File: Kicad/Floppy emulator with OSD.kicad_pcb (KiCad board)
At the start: 2 copper layers, 44.5 x 45.7 mm, 59 parts, among them J1 Display, J10 KBD, J11 Drive Select, J2 SDCARD, J3 Prog, J4 Serial, J5 Prog2, J9 Video, P1 To Computer, P2 POWER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

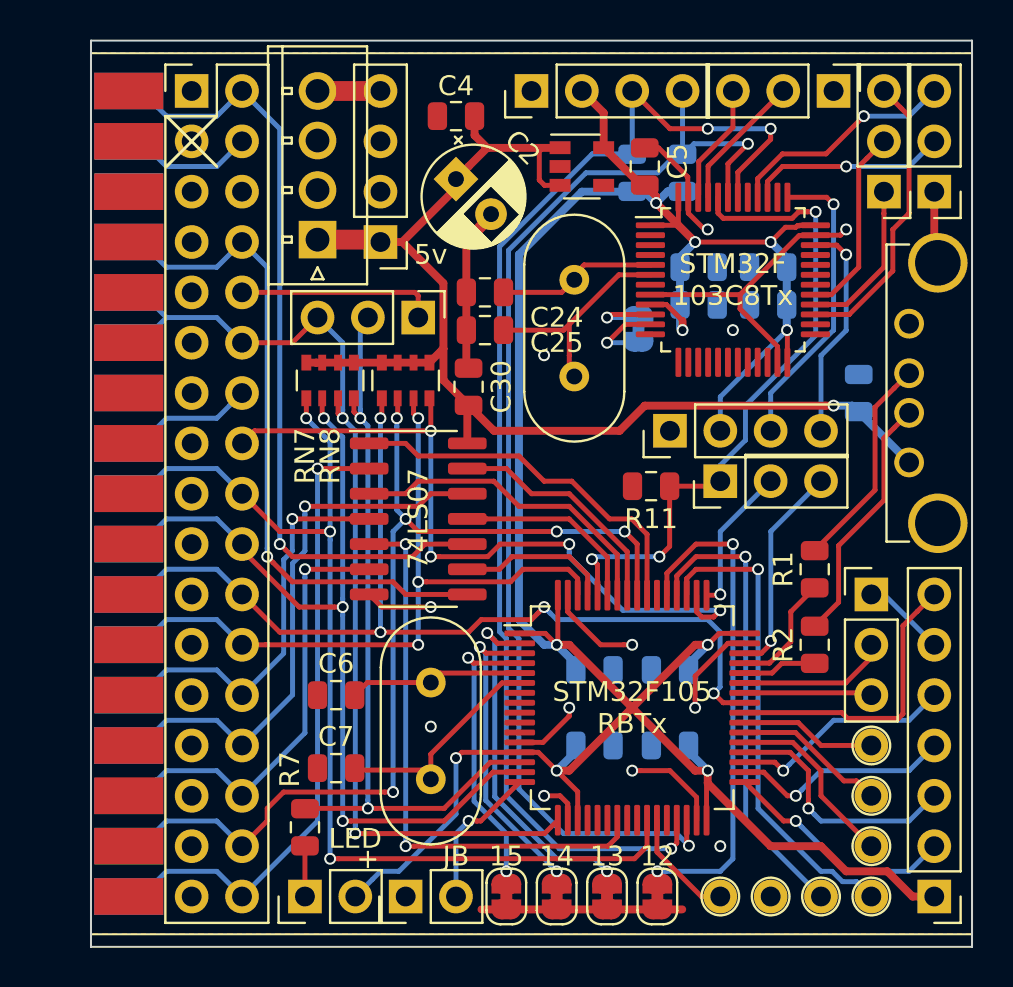
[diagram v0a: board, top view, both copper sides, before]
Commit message: Kicad: conversion to Kicad 6, rework component placement to plug on top of selector and include video resistor. Photo
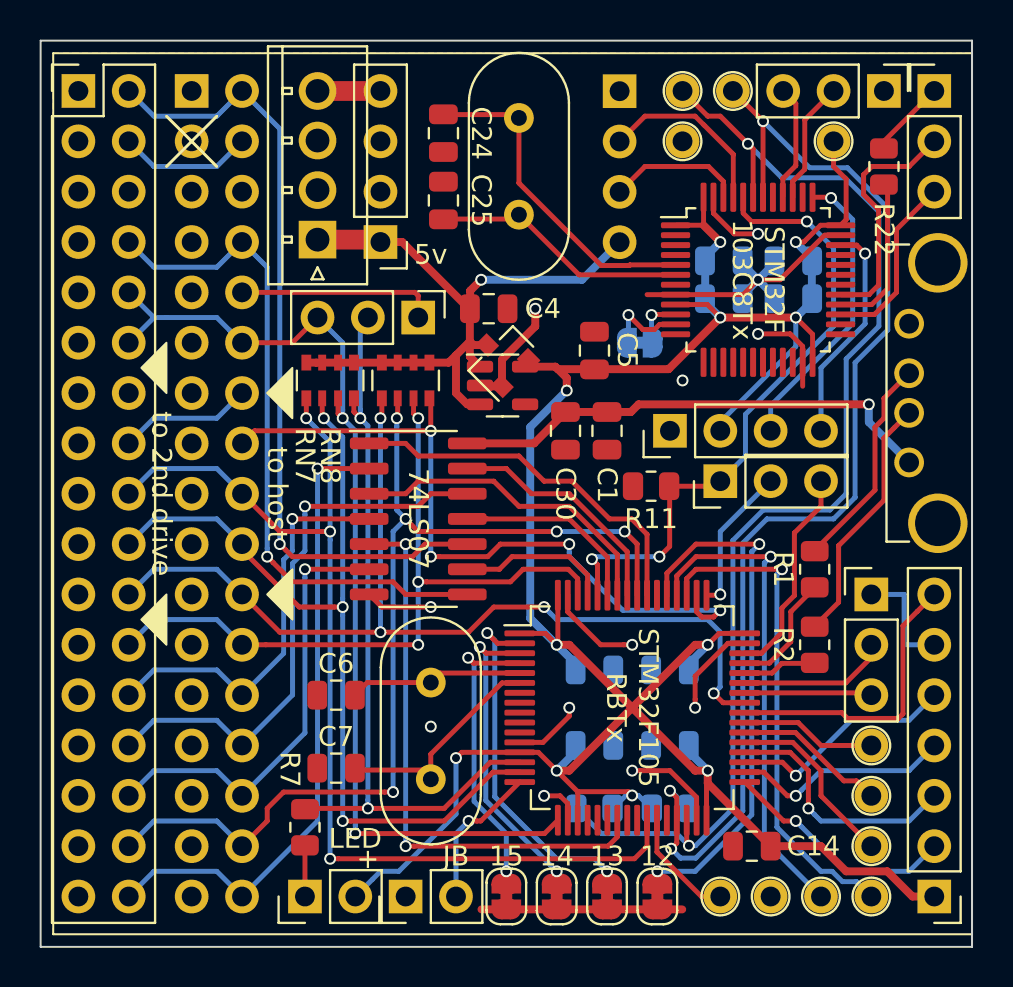
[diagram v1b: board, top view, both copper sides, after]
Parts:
- removed C2: 100u, Capacitor_THT:CP_Radial_D5.0mm_P2.50mm
- removed J1: Display, Connector_PinHeader_2.54mm:PinHeader_1x04_P2.54mm_Vertical
- added C14: 100n, Capacitor_SMD:C_0805_2012Metric, F.Cu at (122.9, 147.3)
- added FID1: Fiducial, Sassa:CC_BY_NC_SA_long_silkscreen, B.Cu at (102.2, 135.3)
- added R22: 270, Resistor_SMD:R_0805_2012Metric, F.Cu at (129.5, 113.0)
- added TP10: TestPoint, Sassa:TestPoint_THTPad_D1.7mm_Drill1.0mm, F.Cu at (121.9, 109.2)
- added TP11: TestPoint, Sassa:TestPoint_THTPad_D1.7mm_Drill1.0mm, F.Cu at (119.4, 111.8)
- added TP8: TestPoint, Sassa:TestPoint_THTPad_D1.7mm_Drill1.0mm, F.Cu at (127.0, 111.8)
- added TP9: TestPoint, Sassa:TestPoint_THTPad_D1.7mm_Drill1.0mm, F.Cu at (119.4, 109.2)
- added U5: XC6206PxxxMR, Sassa:SOT-23, F.Cu at (110.2, 122.7)
- C1: moved to F.Cu
- J11: footprint Connector_PinHeader_2.54mm:PinHeader_1x03_P2.54mm_Vertical -> Connector_PinSocket_2.54mm:PinSocket_1x04_P2.54mm_Vertical; moved to B.Cu
- P1: footprint Connector_PinHeader_2.54mm:PinHeader_2x17_P2.54mm_Vertical -> Connector_PinSocket_2.54mm:PinSocket_2x17_P2.54mm_Vertical; moved to B.Cu
- P4: value To Floppy -> To other Floppy drive; footprint Sassa:Pin_Header_2x17_Female_EdgeMount_Pitch2.54mm -> Connector_PinHeader_2.54mm:PinHeader_2x17_P2.54mm_Vertical; moved to F.Cu
- moved P4 40.7 mm to (88.9, 109.2), turned to 0 degrees
- moved R21 32.4 mm to (114.9, 145.4), turned to 180 degrees
- moved R20 32.1 mm to (118.7, 145.4), turned to 0 degrees
- moved C1 12.8 mm to (115.6, 126.4), turned to -90 degrees
- moved U4 11.8 mm to (110.3, 124.1)
- moved J11 10.8 mm to (116.2, 109.2), turned to 180 degrees
- moved C4 9.85 mm to (109.6, 120.2), turned to 0 degrees
- moved C5 9.63 mm to (114.9, 122.3)
- moved Y20 8.63 mm to (111.1, 110.6)
- moved C24 8.30 mm to (107.3, 111.3), turned to -90 degrees
- moved C25 6.87 mm to (107.3, 114.7), turned to 90 degrees
- moved J10 5.68 mm to (129.5, 109.2), turned to -90 degrees
- moved J9 5.68 mm to (132.1, 109.2), turned to 0 degrees
- moved C30 5.37 mm to (113.5, 126.4), turned to -90 degrees
- moved C21 1.31 mm to (125.0, 117.8)
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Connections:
- net +3V3 renamed +3.3V
- J9 pad 1: VIDEO -> Net-(J9-Pad1)
- P1 pad 6: (no net) -> unconnected-(P1-Pad6)
- P4 pad 14: (no net) -> unconnected-(P4-Pad14)
- P4 pad 6: (no net) -> unconnected-(P4-Pad6)
- U20 pad 12: (no net) -> unconnected-(U20-Pad12)
- U20 pad 13: (no net) -> unconnected-(U20-Pad13)
- U20 pad 14: (no net) -> unconnected-(U20-Pad14)
- U20 pad 15: (no net) -> unconnected-(U20-Pad15)
- U20 pad 16: (no net) -> unconnected-(U20-Pad16)
- U20 pad 17: (no net) -> unconnected-(U20-Pad17)
- U20 pad 18: (no net) -> unconnected-(U20-Pad18)
- U20 pad 19: (no net) -> unconnected-(U20-Pad19)
- U20 pad 2: (no net) -> unconnected-(U20-Pad2)
- U20 pad 20: (no net) -> unconnected-(U20-Pad20)
- U20 pad 21: (no net) -> unconnected-(U20-Pad21)
- U20 pad 22: (no net) -> unconnected-(U20-Pad22)
- U20 pad 25: (no net) -> unconnected-(U20-Pad25)
- U20 pad 26: (no net) -> unconnected-(U20-Pad26)
- U20 pad 3: (no net) -> unconnected-(U20-Pad3)
- U20 pad 30: (no net) -> unconnected-(U20-Pad30)
- U20 pad 31: (no net) -> unconnected-(U20-Pad31)
- U20 pad 32: (no net) -> unconnected-(U20-Pad32)
- U20 pad 33: (no net) -> unconnected-(U20-Pad33)
- U20 pad 38: (no net) -> unconnected-(U20-Pad38)
- U20 pad 4: (no net) -> unconnected-(U20-Pad4)
- U20 pad 41: (no net) -> unconnected-(U20-Pad41)
- U3 pad 10: (no net) -> unconnected-(U3-Pad10)
- U3 pad 11: (no net) -> unconnected-(U3-Pad11)
- U3 pad 20: (no net) -> unconnected-(U3-Pad20)
- U3 pad 21: (no net) -> unconnected-(U3-Pad21)
- U3 pad 22: (no net) -> unconnected-(U3-Pad22)
- U3 pad 24: (no net) -> unconnected-(U3-Pad24)
- U3 pad 25: (no net) -> unconnected-(U3-Pad25)
- U3 pad 28: (no net) -> unconnected-(U3-Pad28)
- U3 pad 54: (no net) -> unconnected-(U3-Pad54)
- U3 pad 8: (no net) -> unconnected-(U3-Pad8)
- U3 pad 9: (no net) -> unconnected-(U3-Pad9)
- U4 pad 4: (no net) -> unconnected-(U4-Pad4)
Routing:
- net Net-(C24-Pad1): track 8.24 -> 16.8 mm
- net KB_CLOCK: track 11.7 -> 5.90 mm, vias 1 -> 0
- net VSYNC: track 14.8 -> 9.15 mm
- net Net-(J9-Pad1): track 0.00 -> 3.95 mm
- net KB_DATA: track 10.0 -> 6.22 mm, vias 1 -> 0
- net SCL: track 62.6 -> 58.8 mm
- net GND: track 72.5 -> 68.7 mm
- net +3.3V: track 140.8 -> 137.1 mm, vias 10 -> 11
- net +5V: track 62.5 -> 59.6 mm, vias 1 -> 2
- net CSYNC_HSYNC: track 9.64 -> 12.3 mm
- net DS_B: track 6.93 -> 9.23 mm
- net Net-(C25-Pad1): track 11.2 -> 13.1 mm
- net SDA: track 59.1 -> 61.0 mm
- net Net-(JP20-Pad1): track 4.34 -> 2.82 mm
- net BOOT0: track 33.4 -> 32.0 mm
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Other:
- board size 44.5 x 45.7 mm -> 47 x 45.7 mm
- net class Default removed
- board text added: "5V"
- board text added: "Changes from 0.1: - Kicad 6 - changed floppy connectors footprints - add 5V to J11 for powering from the floppy selector - change J11 placement to face its equivalent on the floppy selector - moved some components to accommodate these changes - add R22 on video output - correct OSD CK and IO labels that were swapped in prototype"
- board text added: "DT"
- board text added: "FLACO 2020"
- board text added: "FLOPPY+OSD"
- board text added: "https://github.com/f1ac0 /Floppy-emulator-with-OSD"
- board text added: "to 2nd drive"
- board text added: "to host"
- board text added: "v0.2"
- board text removed: "DT/CK"
- board text removed: "ERRATUM: need to add a 270 ohm resistor on the video line in prototype, OSD CK and IO labels were swapped"
- board text removed: "FLACO 2020 v0.1"
- board text removed: "GOTEK+ OSD"
